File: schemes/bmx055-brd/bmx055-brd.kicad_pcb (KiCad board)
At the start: 2 copper layers, 17 parts, among them P1 vcc, P2 gnd, P3 accel-cs, P4 gyro-cs, P5 magnet-cs, P6 sck, P7 mosi, P8 miso, U1 BMX055

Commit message: a
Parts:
- moved P6 41.3 mm to (182.2, 91.2)
- moved P4 38.1 mm to (182.2, 89.0)
- moved P7 36.6 mm to (182.2, 93.5)
- moved P1 35.6 mm to (182.2, 82.2)
- moved P5 34.7 mm to (182.2, 86.8)
- moved P3 26.0 mm to (182.2, 98.0)
- moved P8 22.9 mm to (182.2, 95.8)
- moved P2 22.3 mm to (182.2, 84.5)
- moved R3 12.2 mm to (179.2, 86.8), turned to 180 degrees
- moved R6 11.6 mm to (179.2, 95.8), turned to 180 degrees
- moved R1 7.91 mm to (179.2, 98.0), turned to 180 degrees
- moved R2 5.15 mm to (179.2, 89.0), turned to 180 degrees
- moved R5 1.58 mm to (179.2, 93.5)
- moved C1 1.12 mm to (173.2, 87.2), turned to 90 degrees
- moved C2 0.90 mm to (174.2, 95.8)
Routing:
- net GND: track 0.00 -> 47.7 mm, vias 0 -> 2
- net /miso: track 0.00 -> 22.5 mm
- net VDD: track 0.00 -> 20.3 mm, vias 0 -> 2
- net /~magnet-cs~: track 0.00 -> 11.3 mm
- net /~accel-cs~: track 0.00 -> 10.7 mm
- net /~gyro-cs~: track 0.00 -> 5.55 mm
- net /mosi: track 0.00 -> 3.99 mm
- net /sck: track 0.00 -> 2.64 mm
- net Net-(P8-Pad1): track 0.00 -> 2.05 mm
- net Net-(P7-Pad1): track 0.00 -> 2.05 mm
- net Net-(P6-Pad1): track 0.00 -> 2.05 mm
- net Net-(P5-Pad1): track 0.00 -> 2.05 mm
- net Net-(P4-Pad1): track 0.00 -> 2.05 mm
- net Net-(P3-Pad1): track 0.00 -> 2.05 mm
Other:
- board outline added: 13 x 19 mm

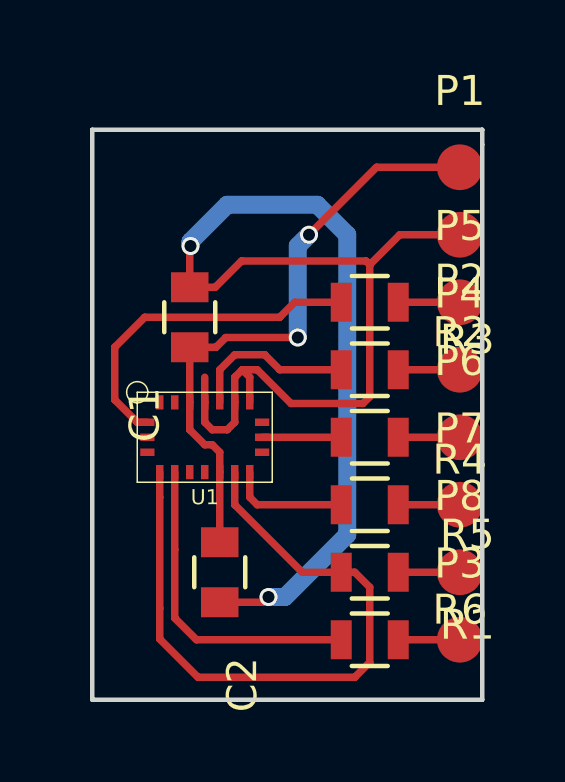
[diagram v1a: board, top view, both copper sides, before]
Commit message: Remade board for I2C mode and prepared for tonner transfer.
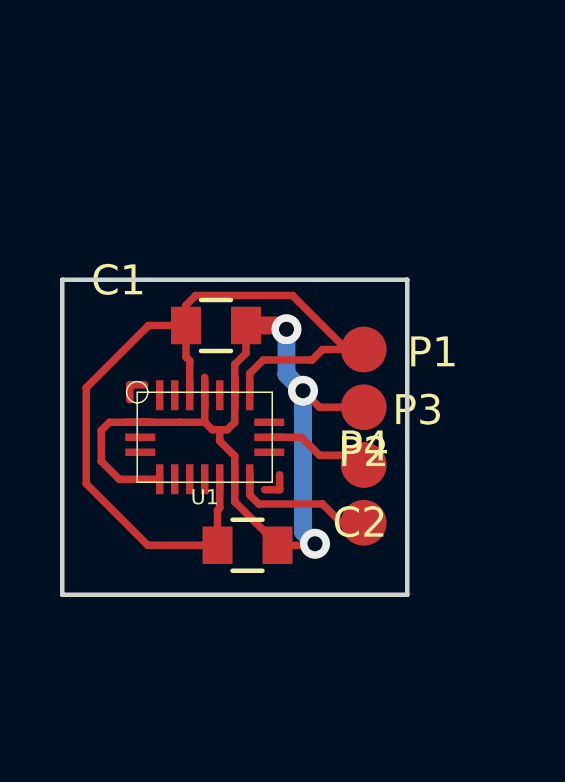
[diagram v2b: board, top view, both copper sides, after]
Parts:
- removed P5: magnet-cs, Measurement_Points:Measurement_Point_Round-SMD-Pad_Small
- removed P6: sck, Measurement_Points:Measurement_Point_Round-SMD-Pad_Small
- removed P7: mosi, Measurement_Points:Measurement_Point_Round-SMD-Pad_Small
- removed P8: miso, Measurement_Points:Measurement_Point_Round-SMD-Pad_Small
- removed R1, R2, R3, R4, R5, R6: 100, Resistors_SMD:R_0805
- P3: value accel-cs -> scl
- P4: value gyro-cs -> sda
- U1: footprint libs:bmx055 -> libs:bmx055-w
- moved P1 6.87 mm to (179.1, 88.3)
- moved P3 6.65 mm to (179.1, 92.2)
- moved P2 6.58 mm to (179.1, 90.2)
- moved P4 6.02 mm to (179.1, 94.1)
- moved C2 1.29 mm to (175.2, 94.8), turned to 0 degrees
- moved C1 0.92 mm to (174.1, 87.5), turned to 0 degrees
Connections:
- P3 pad 1: Net-(P3-Pad1) -> /scl
- P4 pad 1: Net-(P4-Pad1) -> /sda
- U1 pad 11: /mosi -> /sda
- U1 pad 12: /miso -> GND
- U1 pad 16: /~accel-cs~ -> (no net)
- U1 pad 17: /miso -> GND
- U1 pad 20: /~magnet-cs~ -> GND
- U1 pad 5: /~gyro-cs~ -> (no net)
- U1 pad 7: GND -> VDD
- U1 pad 9: /sck -> /scl
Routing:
- net /miso: track 22.5 -> 0.00 mm
- net GND: track 47.7 -> 31.1 mm, vias 2 -> 3
- net /~magnet-cs~: track 11.3 -> 0.00 mm
- net /~accel-cs~: track 10.7 -> 0.00 mm
- net VDD: track 20.3 -> 29.6 mm, vias 2 -> 0
- net /~gyro-cs~: track 5.55 -> 0.00 mm
- net /sda: track 0.00 -> 5.05 mm
- net /mosi: track 3.99 -> 0.00 mm
- net /scl: track 0.00 -> 3.53 mm
- net /sck: track 2.64 -> 0.00 mm
- net Net-(P8-Pad1): track 2.05 -> 0.00 mm
- net Net-(P7-Pad1): track 2.05 -> 0.00 mm
- net Net-(P6-Pad1): track 2.05 -> 0.00 mm
- net Net-(P5-Pad1): track 2.05 -> 0.00 mm
- net Net-(P4-Pad1): track 2.05 -> 0.00 mm
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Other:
- board size 13 x 19 mm -> 11.5 x 10.5 mm
